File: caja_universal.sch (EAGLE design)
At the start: 34 parts, among them IC2 AD620N, IC3 TL084P, IC4 TL084P, IC5 LM317LD, IC6 LM318N

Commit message: Esquematico finalizado (v0), board en progreso
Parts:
- removed IC2: AD620N, analog-devices:AD620N
- removed IC5: LM317LD, linear:LM317LD
- removed IC6: LM318N, linear:LM318N
- removed JP10, JP11, JP12: (no value), pinhead:PINHD-1X1
- removed JP4, JP5, JP8, JP9: (no value), pinhead:PINHD-1X2
- removed R12, R2: (no value), resistor:R-US_0204/7
- added BNC-HALL, BNC-HR, BNC-PRESION, BNC-TENSION: (no value), pinhead:PINHD-1X2
- added HALL-PLACA, HR-PLACA, TENSION-PLACA: (no value), pinhead:PINHD-1X1
- added LM385-OFFSET: 2SC945, transistor:2SC945
- added POT-GAIN, POT-OFFSET: (no value), pinhead:PINHD-1X3
- added PREAMP-PRESION: AD620N, analog-devices:AD620N
- added R-REG-FCORR: 10k, resistor:R-US_0204/7
- added R-REG-OFFSET: 680k, resistor:R-US_0204/7
- added SEGUIDOS-PREAMP-PRESION: LM318N, linear:LM318N
- R10, R7, R8, R9: value (none) -> 10k
- R3, R4: value (none) -> 20k
- R5: value (none) -> 1k
- R6: value (none) -> 2k
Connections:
- new net -1.25V: IC3C.-IN, IC3C.OUT, POT-OFFSET.3
- new net 1.25V: IC3A.-IN, IC3A.OUT, POT-OFFSET.2, R3.1
- new net HALL: BNC-HALL.1, HALL-PLACA.1
- new net HR: BNC-HR.1, HR-PLACA.1
- new net N$10: IC3D.-IN, R5.2, R6.1
- new net N$11: IC3D.OUT, IC4A.+IN, R6.2
- new net N$12: IC4B.-IN, R10.2, R7.1, R9.2
- new net N$13: R9.1, SEGUIDOS-PREAMP-PRESION.-IN, SEGUIDOS-PREAMP-PRESION.OUT
- new net N$14: IC4B.OUT, IC4C.+IN, R7.2
- new net N$15: IC4C.-IN, IC4C.OUT, R8.1
- new net N$16: IC4D.-IN, POT-GAIN.3, R8.2
- new net N$6: IC3B.-IN, R3.2, R4.1
- new net N$7: IC3A.+IN, LM385-OFFSET.C, R-REG-OFFSET.2
- new net N$8: IC3B.OUT, IC3C.+IN, R4.2
- new net N$9: IC4A.-IN, IC4A.OUT, R10.1
- new net OFFSET: IC3D.+IN, POT-OFFSET.1
- new net PRESION: BNC-PRESION.1, IC4D.OUT, POT-GAIN.2
- new net TENSION: BNC-TENSION.1, TENSION-PLACA.1
- net +12V: now also PREAMP-PRESION.+V, R-REG-FCORR.2, R-REG-OFFSET.1, SEGUIDOS-PREAMP-PRESION.V+; no longer IC2.+V
- net -12V: now also PREAMP-PRESION.-V, SEGUIDOS-PREAMP-PRESION.V-; no longer IC2.-V
- net 0V: now also BNC-HALL.2, BNC-HR.2, BNC-PRESION.2, BNC-TENSION.2, IC3B.+IN, IC4B.+IN, LM385-OFFSET.B, LM385-OFFSET.E, PREAMP-PRESION.REF, R5.1; no longer IC2.REF
- net N$3: now also R-REG-FCORR.1
- net N$4: now also PREAMP-PRESION.RG@1; no longer IC2.RG@1
- net N$5: now also PREAMP-PRESION.RG@2; no longer IC2.RG@2
- net P+: now also PREAMP-PRESION.+; no longer IC2.+
- net P-: now also PREAMP-PRESION.-; no longer IC2.-
- net PRESION-PREAMP: now also PREAMP-PRESION.OUT, SEGUIDOS-PREAMP-PRESION.+IN; no longer IC2.OUT
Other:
- moved on the sheet: ALIMENTACION-BATERIAS, CHECK, CHECK-LED, IC3A, IC3B, IC3C, IC3D, IC4A, IC4B, IC4C, IC4D, PRESION-PLACA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

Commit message: Terminada primera version de la placa
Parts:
- removed LM385-FCORR, LM385-OFFSET: 2SC945, transistor:2SC945
- removed OPAMP-FCORR, SEGUIDOS-PREAMP-PRESION: LM318N, linear:LM318N
- removed R-REG-FCORR: 10k, resistor:R-US_0204/7
- removed TENSION-PLACA: (no value), pinhead:PINHD-1X1
- added +12V-FUSE, -12V-FUSE, T-PLACA: (no value), pinhead:PINHD-1X2
- added D1, D2: LM385, lm385:LM385
- added IC1, IC5: NE5534AN, linear:NE5534AN
- added R11: 10k, resistor:R-US_0204/7
- added SWITCH-P: (no value), pinhead:PINHD-1X4
- BNC-HALL, BNC-HR, BNC-PRESION, BNC-TENSION: value (none) -> A1944-50; device pinhead:PINHD-1X2 -> con-coax:A1944-50
- HALL-PLACA, HR-PLACA: device pinhead:PINHD-1X1 -> pinhead:PINHD-1X2
- renumbered ALIMENTACION-BATERIAS to V-BAT, ALIMENTACION-PLACA to V-PLACA, CORRIENTE-PLACA to I-PLACA, PREAMP-PRESION to IC2, PRESION-PLACA to P-PLACA, R-FCORR to R2, R-REG-OFFSET to R12, RG-PRESION to R1, SWITCH to SWITCH-GRAL
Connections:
- net PRESION renamed POUT
- removed net 0VBAT: V-BAT.2
- removed net PRESION-PREAMP: IC2.OUT, SEGUIDOS-PREAMP-PRESION.+IN
- new net +12V-PRESION: CHECK.1, IC1.V+, IC2.+V, IC5.V+, R11.2, R12.1, SWITCH-P.2
- new net +12VFUSE: +12V-FUSE.1, SWITCH-GRAL.1
- new net -12V-PRESION: IC1.V-, IC2.-V, IC5.V-, SWITCH-P.4
- new net -12VFUSE: -12V-FUSE.1, SWITCH-GRAL.3
- new net P-PREAMP: IC2.OUT, IC5.+IN
- net +12V: now also +12V-FUSE.2, SWITCH-P.1; no longer CHECK.1, IC2.+V, OPAMP-FCORR.V+, R-REG-FCORR.2, R12.1, SEGUIDOS-PREAMP-PRESION.V+, SWITCH-GRAL.1
- net +I: now also IC1.OUT; no longer OPAMP-FCORR.OUT
- net -12V: now also -12V-FUSE.2, SWITCH-P.3; no longer IC2.-V, OPAMP-FCORR.V-, SEGUIDOS-PREAMP-PRESION.V-, SWITCH-GRAL.3
- net -I: now also IC1.-IN; no longer OPAMP-FCORR.-IN
- net 0V: now also D1.-, D1.FB, D2.-, D2.FB, V-BAT.2; no longer LM385-FCORR.B, LM385-FCORR.E, LM385-OFFSET.B, LM385-OFFSET.E
- net HALL: now also HALL-PLACA.2; no longer HALL-PLACA.1
- net HR: now also HR-PLACA.2; no longer HR-PLACA.1
- net N$13: now also IC5.-IN, IC5.OUT; no longer SEGUIDOS-PREAMP-PRESION.-IN, SEGUIDOS-PREAMP-PRESION.OUT
- net N$3: now also D2.+, IC1.+IN, R11.1; no longer LM385-FCORR.C, OPAMP-FCORR.+IN, R-REG-FCORR.1
- net N$7: now also D1.+; no longer LM385-OFFSET.C
- net TENSION: now also T-PLACA.2; no longer TENSION-PLACA.1

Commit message: Version para revisar (JyG)
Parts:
- IC1, IC5: value NE5534AN -> AD711N; device linear:NE5534AN -> analog-devices:AD711N
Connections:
- net +12V-PRESION: now also IC1.+VS, IC5.+VS; no longer IC1.V+, IC5.V+
- net -12V-PRESION: now also IC1.-VS, IC5.-VS; no longer IC1.V-, IC5.V-
- net -I: now also IC1.IN-; no longer IC1.-IN
- net N$13: now also IC5.IN-; no longer IC5.-IN
- net N$3: now also IC1.IN+; no longer IC1.+IN
- net P-PREAMP: now also IC5.IN+; no longer IC5.+IN
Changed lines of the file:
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@@
 <part name="RCHECK" library="resistor" deviceset="R-US_" device="0204/7" value="100k"/>
 <part name="CHECK-LED" library="pinhead" deviceset="PINHD-1X2" device=""/>
-<part name="IC1" library="linear" deviceset="NE5534" device="N" technology="A" value="NE5534AN"/>
-<part name="IC5" library="linear" deviceset="NE5534" device="N" technology="A" value="NE5534AN"/>
 <part name="POT-OFFSET" library="pinhead" deviceset="PINHD-1X3" device=""/>
 <part name="POT-GAIN" library="pinhead" deviceset="PINHD-1X3" device=""/>
@@
 <part name="D1" library="lm385" deviceset="LM385" device=""/>
 <part name="D2" library="lm385" deviceset="LM385" device=""/>
+<part name="IC1" library="analog-devices" deviceset="AD711" device="N"/>
+<part name="IC5" library="analog-devices" deviceset="AD711" device="N"/>
 </parts>
 <sheets>
@@
 <instance part="RCHECK" gate="G$1" x="-17.78" y="63.5"/>
 <instance part="CHECK-LED" gate="G$1" x="2.54" y="60.96"/>
-<instance part="IC1" gate="A" x="96.52" y="104.14"/>
-<instance part="IC5" gate="A" x="223.52" y="33.02"/>
 <instance part="POT-OFFSET" gate="A" x="248.92" y="139.7" rot="R180"/>
 <instance part="POT-GAIN" gate="A" x="370.84" y="25.4" rot="R270"/>
@@
 <instance part="D1" gate="G$1" x="210.82" y="104.14" rot="R270"/>
 <instance part="D2" gate="G$1" x="73.66" y="99.06" rot="R270"/>
+<instance part="IC1" gate="G$1" x="104.14" y="104.14"/>
+<instance part="IC5" gate="G$1" x="223.52" y="33.02"/>
 </instances>
 <busses>
@@
 </segment>
 <segment>
-<pinref part="IC1" gate="A" pin="V+"/>
-<wire x1="93.98" y1="111.76" x2="93.98" y2="116.84" width="0.1524" layer="91"/>
-<label x="93.98" y="116.84" size="1.778" layer="95"/>
-</segment>
-<segment>
 <pinref part="IC2" gate="G$1" pin="+V"/>
 <wire x1="96.52" y1="53.34" x2="96.52" y2="60.96" width="0.1524" layer="91"/>
@@
 </segment>
 <segment>
-<pinref part="IC5" gate="A" pin="V+"/>
-<wire x1="220.98" y1="40.64" x2="220.98" y2="43.18" width="0.1524" layer="91"/>
-<label x="220.98" y="43.18" size="1.778" layer="95"/>
-</segment>
-<segment>
 <pinref part="SWITCH-P" gate="A" pin="2"/>
 <wire x1="20.32" y1="91.44" x2="33.02" y2="91.44" width="0.1524" layer="91"/>
 <label x="25.4" y="91.44" size="1.778" layer="95"/>
+</segment>
+<segment>
+<pinref part="IC1" gate="G$1" pin="+VS"/>
+<wire x1="104.14" y1="114.3" x2="104.14" y2="124.46" width="0.1524" layer="91"/>
+<label x="104.14" y="124.46" size="1.778" layer="95"/>
+</segment>
+<segment>
+<pinref part="IC5" gate="G$1" pin="+VS"/>
+<wire x1="223.52" y1="43.18" x2="223.52" y2="48.26" width="0.1524" layer="91"/>
+<label x="223.52" y="48.26" size="1.778" layer="95"/>
 </segment>
 </net>
@@
 <net name="-12V-PRESION" class="0">
 <segment>
-<pinref part="IC1" gate="A" pin="V-"/>
-<wire x1="93.98" y1="96.52" x2="93.98" y2="93.98" width="0.1524" layer="91"/>
-<label x="93.98" y="93.98" size="1.778" layer="95"/>
+<pinref part="IC1" gate="G$1" pin="-VS"/>
+<wire x1="104.14" y1="93.98" x2="104.14" y2="88.9" width="0.1524" layer="91"/>
+<label x="104.14" y="88.9" size="1.778" layer="95"/>
 </segment>
 <segment>
@@
 </segment>
 <segment>
-<pinref part="IC5" gate="A" pin="V-"/>
-<wire x1="220.98" y1="25.4" x2="220.98" y2="22.86" width="0.1524" layer="91"/>
-<label x="220.98" y="22.86" size="1.778" layer="95"/>
-</segment>
-<segment>
 <pinref part="SWITCH-P" gate="A" pin="4"/>
 <wire x1="20.32" y1="86.36" x2="33.02" y2="86.36" width="0.1524" layer="91"/>
 <label x="25.4" y="86.36" size="1.778" layer="95"/>
 </segment>
+<segment>
+<pinref part="IC5" gate="G$1" pin="-VS"/>
+<wire x1="223.52" y1="22.86" x2="223.52" y2="15.24" width="0.1524" layer="91"/>
+<label x="223.52" y="15.24" size="1.778" layer="95"/>
+</segment>
 </net>
 <net name="+12VBAT" class="0">
@@
 <net name="N$3" class="0">
 <segment>
-<wire x1="88.9" y1="106.68" x2="71.12" y2="106.68" width="0.1524" layer="91"/>
-<pinref part="IC1" gate="A" pin="+IN"/>
 <pinref part="R11" gate="G$1" pin="1"/>
+<wire x1="83.82" y1="106.68" x2="71.12" y2="106.68" width="0.1524" layer="91"/>
 <wire x1="71.12" y1="114.3" x2="71.12" y2="106.68" width="0.1524" layer="91"/>
 <pinref part="D2" gate="G$1" pin="+"/>
 <wire x1="71.12" y1="104.14" x2="71.12" y2="106.68" width="0.1524" layer="91"/>
 <junction x="71.12" y="106.68"/>
+<pinref part="IC1" gate="G$1" pin="IN+"/>
+<wire x1="99.06" y1="106.68" x2="83.82" y2="106.68" width="0.1524" layer="91"/>
 </segment>
 </net>
 <net name="-I" class="0">
 <segment>
-<pinref part="IC1" gate="A" pin="-IN"/>
 <pinref part="R2" gate="G$1" pin="2"/>
-<wire x1="88.9" y1="101.6" x2="83.82" y2="101.6" width="0.1524" layer="91"/>
-<wire x1="83.82" y1="101.6" x2="83.82" y2="91.44" width="0.1524" layer="91"/>
 <wire x1="83.82" y1="91.44" x2="83.82" y2="88.9" width="0.1524" layer="91"/>
 <wire x1="83.82" y1="91.44" x2="124.46" y2="91.44" width="0.1524" layer="91"/>
@@
 <pinref part="I-PLACA" gate="G$1" pin="2"/>
 <wire x1="124.46" y1="101.6" x2="132.08" y2="101.6" width="0.1524" layer="91"/>
+<pinref part="IC1" gate="G$1" pin="IN-"/>
+<wire x1="99.06" y1="101.6" x2="83.82" y2="101.6" width="0.1524" layer="91"/>
+<wire x1="83.82" y1="101.6" x2="83.82" y2="91.44" width="0.1524" layer="91"/>
 </segment>
 </net>
 <net name="+I" class="0">
 <segment>
-<pinref part="IC1" gate="A" pin="OUT"/>
-<wire x1="104.14" y1="104.14" x2="132.08" y2="104.14" width="0.1524" layer="91"/>
 <label x="124.46" y="104.14" size="1.778" layer="95"/>
 <pinref part="I-PLACA" gate="G$1" pin="1"/>
+<wire x1="114.3" y1="104.14" x2="132.08" y2="104.14" width="0.1524" layer="91"/>
+<pinref part="IC1" gate="G$1" pin="OUT"/>
 </segment>
 </net>
@@
 </segment>
 <segment>
-<pinref part="IC5" gate="A" pin="+IN"/>
-<wire x1="215.9" y1="35.56" x2="208.28" y2="35.56" width="0.1524" layer="91"/>
+<wire x1="218.44" y1="35.56" x2="208.28" y2="35.56" width="0.1524" layer="91"/>
 <label x="193.04" y="35.56" size="1.778" layer="95"/>
+<pinref part="IC5" gate="G$1" pin="IN+"/>
 </segment>
 </net>
@@
 <net name="N$13" class="0">
 <segment>
-<pinref part="IC5" gate="A" pin="-IN"/>
-<wire x1="215.9" y1="30.48" x2="213.36" y2="30.48" width="0.1524" layer="91"/>
-<wire x1="213.36" y1="30.48" x2="213.36" y2="20.32" width="0.1524" layer="91"/>
-<wire x1="213.36" y1="20.32" x2="238.76" y2="20.32" width="0.1524" layer="91"/>
 <wire x1="238.76" y1="20.32" x2="238.76" y2="33.02" width="0.1524" layer="91"/>
-<pinref part="IC5" gate="A" pin="OUT"/>
-<wire x1="238.76" y1="33.02" x2="231.14" y2="33.02" width="0.1524" layer="91"/>
+<wire x1="238.76" y1="33.02" x2="233.68" y2="33.02" width="0.1524" layer="91"/>
 <pinref part="R9" gate="G$1" pin="1"/>
 <wire x1="246.38" y1="33.02" x2="238.76" y2="33.02" width="0.1524" layer="91"/>
 <junction x="238.76" y="33.02"/>
-</segment>
-</net>
+<pinref part="IC5" gate="G$1" pin="OUT"/>
+<wire x1="213.36" y1="30.48" x2="213.36" y2="20.32" width="0.1524" layer="91"/>
+<wire x1="218.44" y1="30.48" x2="213.36" y2="30.48" width="0.1524" layer="91"/>
+<pinref part="IC5" gate="G$1" pin="IN-"/>
+<wire x1="238.76" y1="20.32" x2="213.36" y2="20.32" width="0.1524" layer="91"/>
+</segment>
+</net>

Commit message: Agregamos con Juan uno GND que faltaban. Falta ver alimentacion de TL084 y cambiar valor resistencia del LED
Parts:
- added IC6: TL084P, linear:TL084P
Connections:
- net 0V: now also IC4D.+IN, POT-GAIN.1

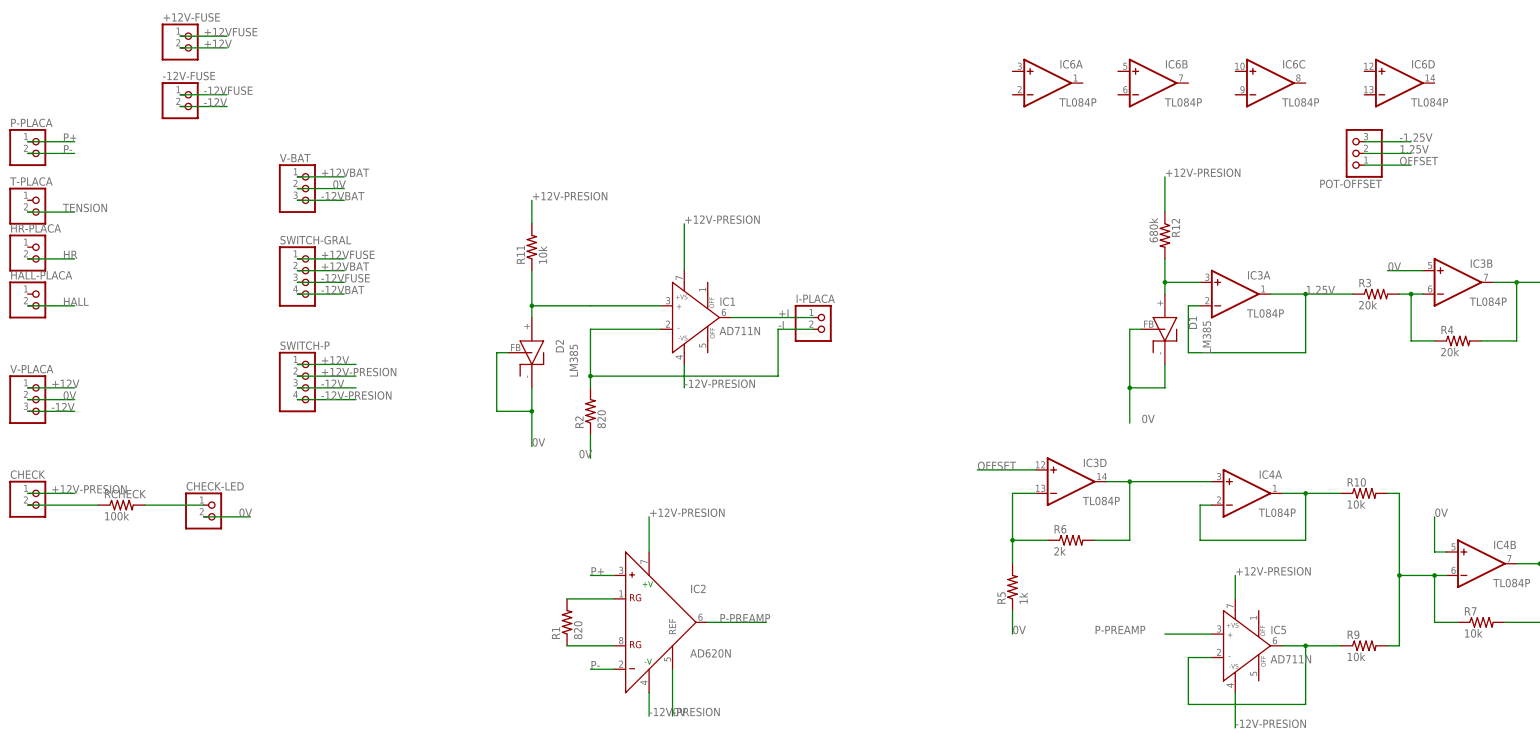
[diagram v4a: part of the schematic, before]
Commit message: corregimos alimentacion TL084
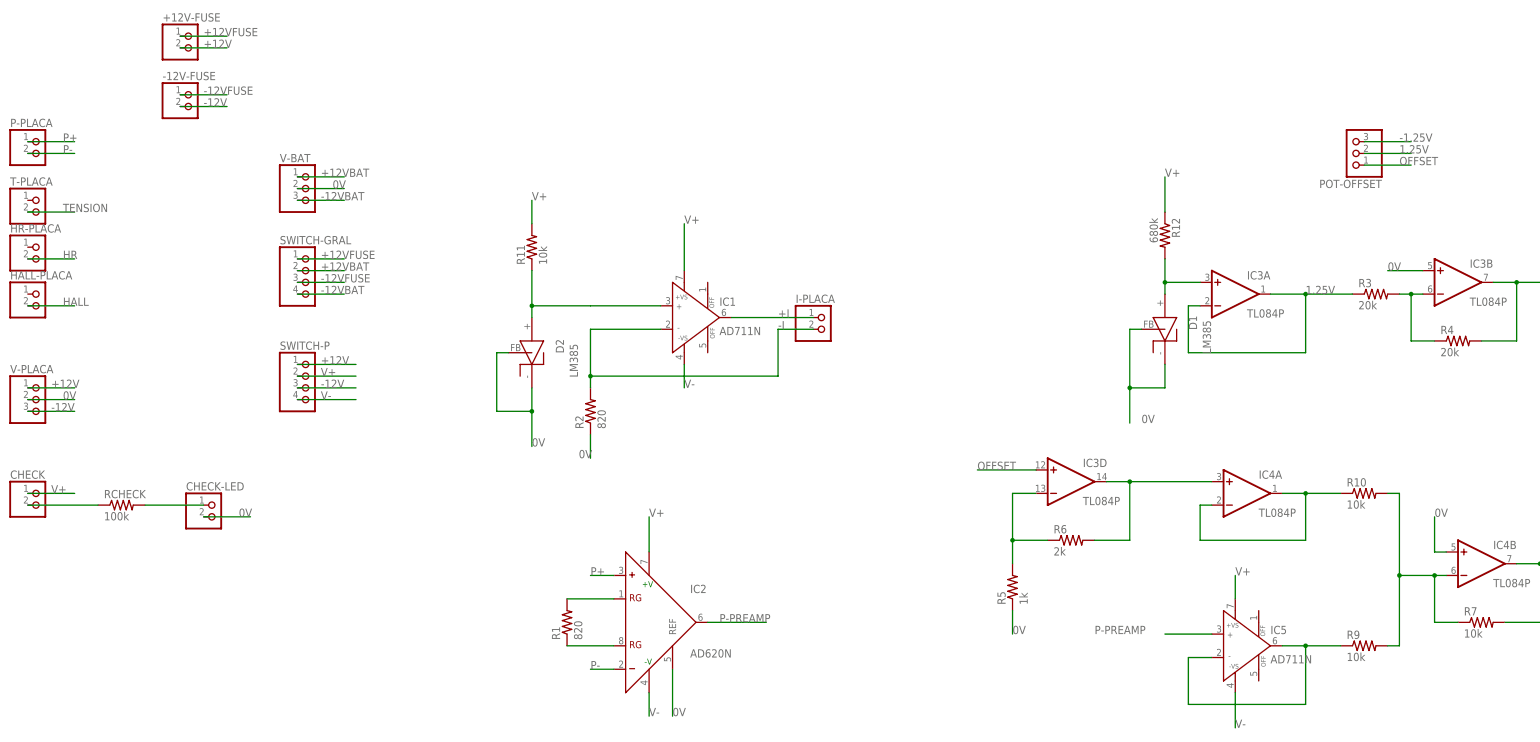
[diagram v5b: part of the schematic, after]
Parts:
- removed IC6: TL084P, linear:TL084P
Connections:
- net +12V-PRESION renamed V+
- net -12V-PRESION renamed V-
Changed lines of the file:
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@@
 <part name="IC1" library="analog-devices" deviceset="AD711" device="N"/>
 <part name="IC5" library="analog-devices" deviceset="AD711" device="N"/>
-<part name="IC6" library="linear" library_urn="urn:adsk.eagle:library:262" deviceset="TL084" device="P" package3d_urn="urn:adsk.eagle:package:16407/2"/>
 </parts>
 <sheets>
@@
 <attribute name="VALUE" x="231.14" y="29.21" size="1.778" layer="96"/>
 </instance>
-<instance part="IC6" gate="A" x="182.88" y="154.94" smashed="yes">
-<attribute name="NAME" x="185.42" y="158.115" size="1.778" layer="95"/>
-<attribute name="VALUE" x="185.42" y="149.86" size="1.778" layer="96"/>
-</instance>
-<instance part="IC6" gate="B" x="205.74" y="154.94" smashed="yes">
-<attribute name="NAME" x="208.28" y="158.115" size="1.778" layer="95"/>
-<attribute name="VALUE" x="208.28" y="149.86" size="1.778" layer="96"/>
-</instance>
-<instance part="IC6" gate="C" x="231.14" y="154.94" smashed="yes">
-<attribute name="NAME" x="233.68" y="158.115" size="1.778" layer="95"/>
-<attribute name="VALUE" x="233.68" y="149.86" size="1.778" layer="96"/>
-</instance>
-<instance part="IC6" gate="D" x="259.08" y="154.94" smashed="yes">
-<attribute name="NAME" x="261.62" y="158.115" size="1.778" layer="95"/>
-<attribute name="VALUE" x="261.62" y="149.86" size="1.778" layer="96"/>
-</instance>
 </instances>
 <busses>
 </busses>
 <nets>
-<net name="+12V-PRESION" class="0">
+<net name="V+" class="0">
 <segment>
 <pinref part="CHECK" gate="G$1" pin="1"/>
@@
 </segment>
 </net>
-<net name="-12V-PRESION" class="0">
+<net name="V-" class="0">
 <segment>
 <pinref part="IC1" gate="G$1" pin="-VS"/>
@@
 </schematic>
 </drawing>
-<compatibility>
-<note version="8.2" severity="warning">
-Since Version 8.2, EAGLE supports online libraries. The ids
-of those online libraries will not be understood (or retained)
-with this version.
-</note>
-<note version="8.3" severity="warning">
-Since Version 8.3, EAGLE supports URNs for individual library
-assets (packages, symbols, and devices). The URNs of those assets
-will not be understood (or retained) with this version.
-</note>
-<note version="8.3" severity="warning">
-Since Version 8.3, EAGLE supports the association of 3D packages
-with devices in libraries, schematics, and board files. Those 3D
-packages will not be understood (or retained) with this version.
-</note>
-</compatibility>
 </eagle>
